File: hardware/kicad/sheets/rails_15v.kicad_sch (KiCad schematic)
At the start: 31 parts, among them U10 ADP7182AUJZ, U8 ADP5071AREZ, U9 ADP7142AUJZ

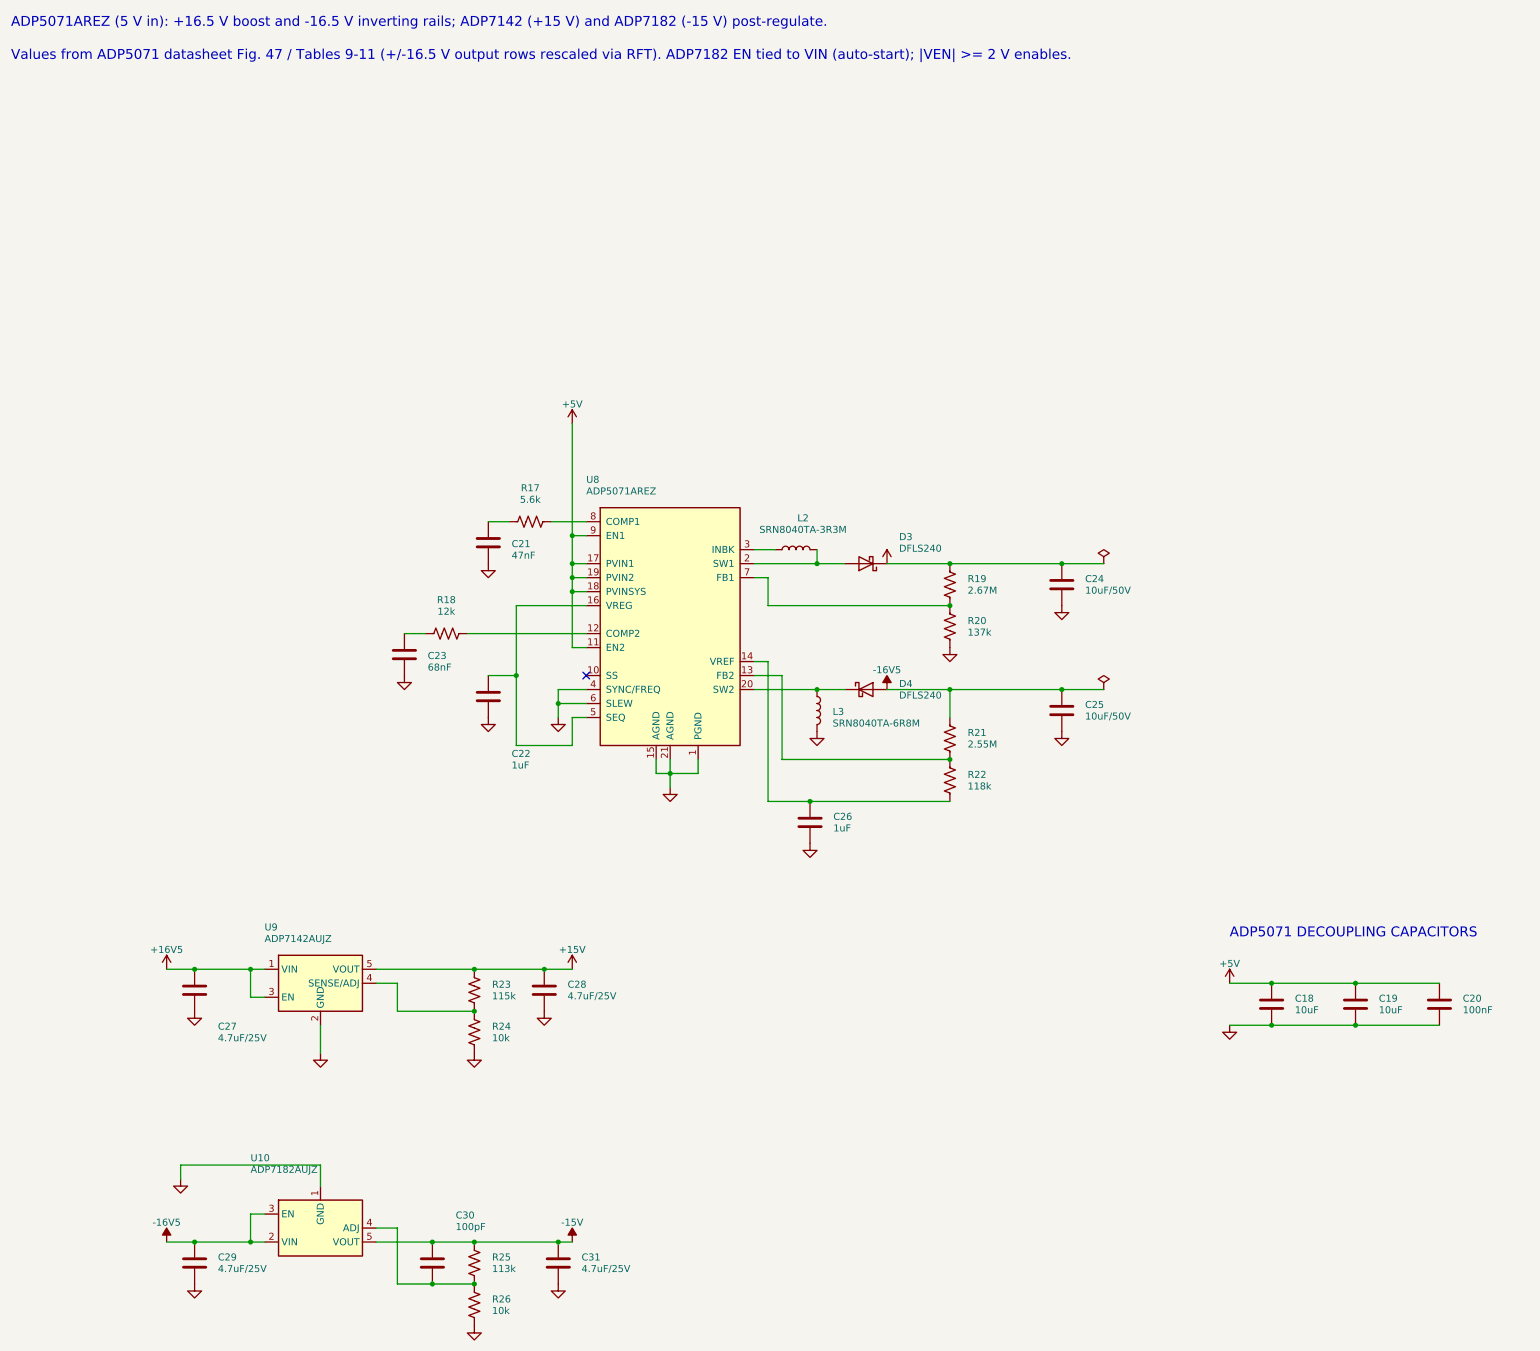
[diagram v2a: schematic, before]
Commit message: Fixing the UUID issues
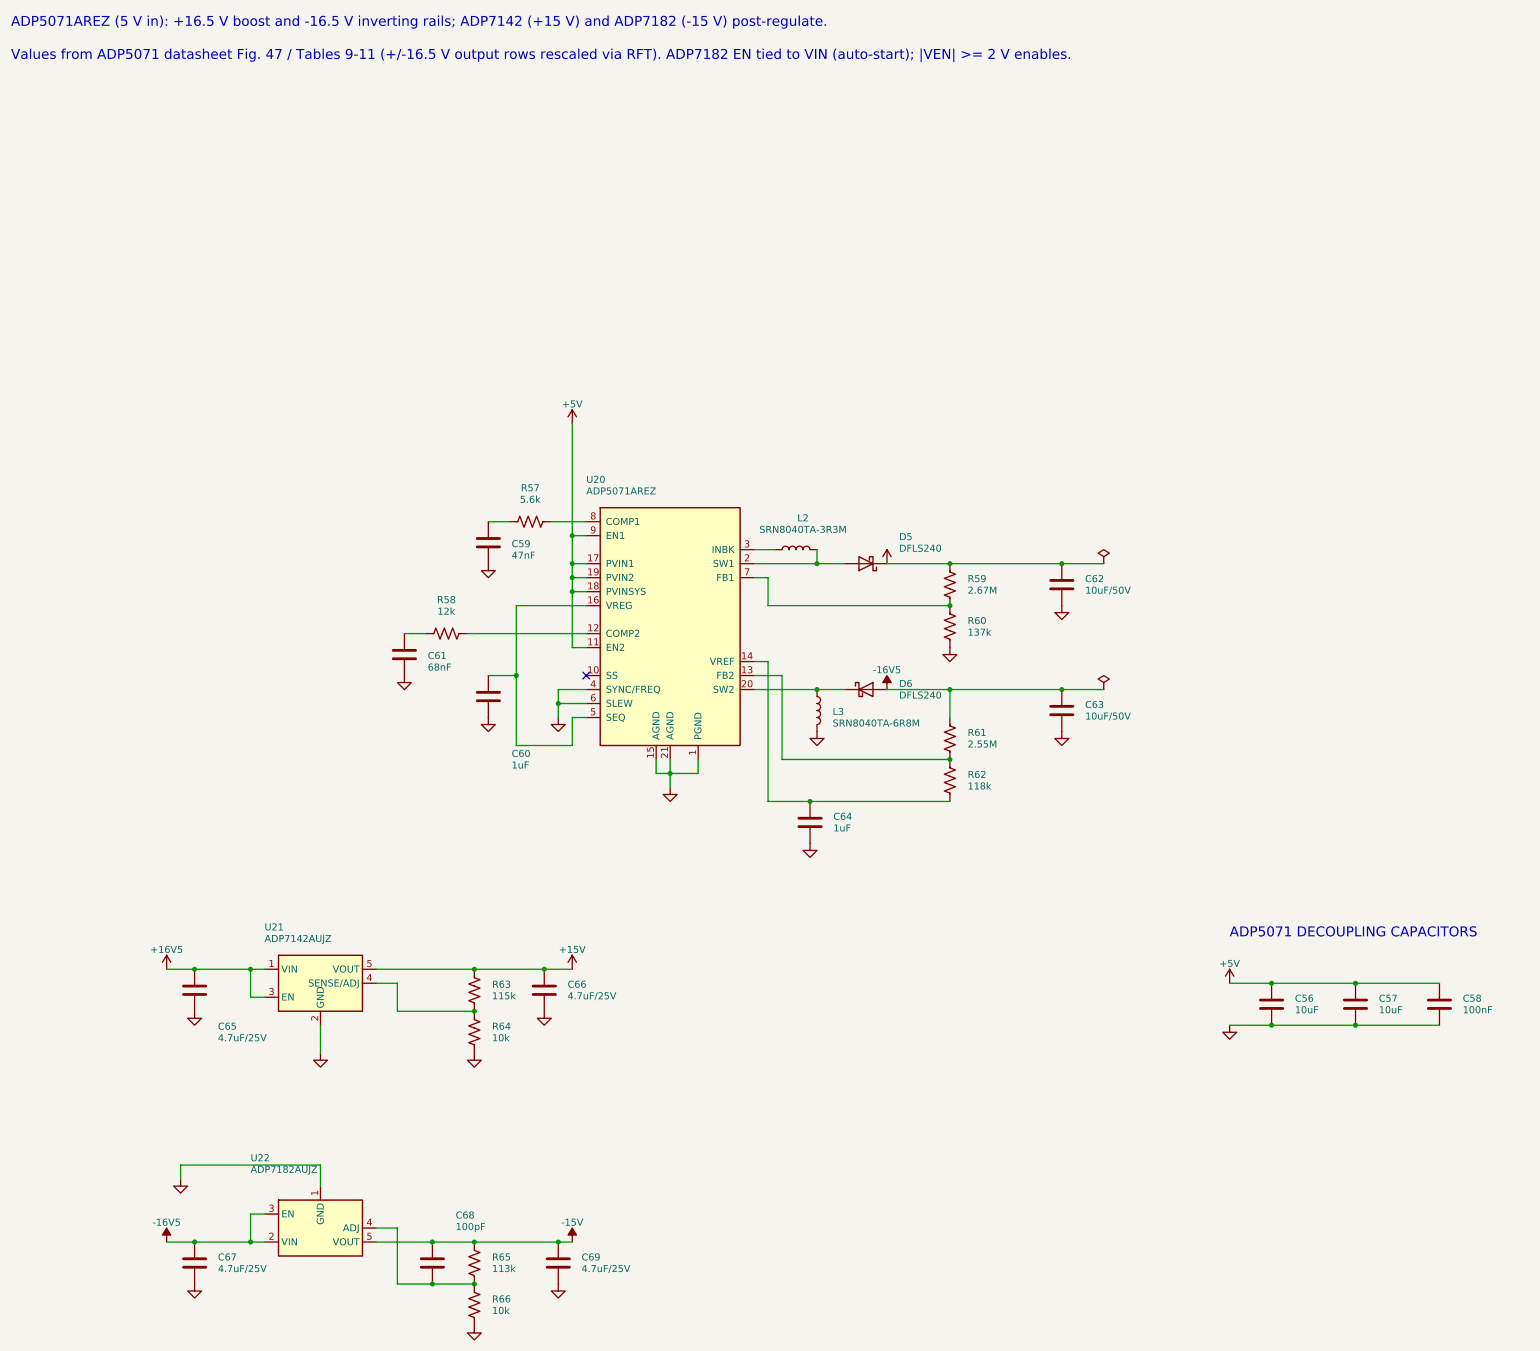
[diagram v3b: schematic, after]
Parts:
- removed C18, C19: 10uF, Capacitor_SMD:C_0805_2012Metric, symbol Device:C
- removed C20: 100nF, Capacitor_SMD:C_0603_1608Metric, symbol Device:C
- removed C21: 47nF, Capacitor_SMD:C_1206_3216Metric, symbol Device:C
- removed C22, C26: 1uF, Capacitor_SMD:C_0805_2012Metric, symbol Device:C
- removed C23: 68nF, Capacitor_SMD:C_1206_3216Metric, symbol Device:C
- removed C24, C25: 10uF/50V, Capacitor_SMD:C_1210_3225Metric, symbol Device:C
- removed C27, C28, C29, C31: 4.7uF/25V, Capacitor_SMD:C_1206_3216Metric, symbol Device:C
- removed C30: 100pF, Capacitor_SMD:C_1206_3216Metric, symbol Device:C
- removed D3, D4: DFLS240, Diode_SMD:D_PowerDI-123, symbol Device:D_Schottky
- removed R17: 5.6k, Resistor_SMD:R_0603_1608Metric, symbol Device:R_US
- removed R18: 12k, Resistor_SMD:R_0603_1608Metric, symbol Device:R_US
- removed R19: 2.67M, Resistor_SMD:R_0603_1608Metric, symbol Device:R_US
- removed R20: 137k, Resistor_SMD:R_0603_1608Metric, symbol Device:R_US
- removed R21: 2.55M, Resistor_SMD:R_0603_1608Metric, symbol Device:R_US
- removed R22: 118k, Resistor_SMD:R_0603_1608Metric, symbol Device:R_US
- removed R23: 115k, Resistor_SMD:R_0603_1608Metric, symbol Device:R_US
- removed R24, R26: 10k, Resistor_SMD:R_0603_1608Metric, symbol Device:R_US
- removed R25: 113k, Resistor_SMD:R_0603_1608Metric, symbol Device:R_US
- removed U10: ADP7182AUJZ, Package_TO_SOT_SMD:TSOT-23-5, symbol Regulator_Linear:ADP7182AUJZ
- removed U8: ADP5071AREZ, Package_SO:ETSSOP-20-1EP_4.4x6.5mm_P0.65mm_EP3x4.2mm, symbol Regulator_Switching:ADP5071AREZ
- removed U9: ADP7142AUJZ, Package_TO_SOT_SMD:TSOT-23-5, symbol Regulator_Linear:ADP7142AUJZ
- added C56, C57: 10uF, Capacitor_SMD:C_0805_2012Metric, symbol Device:C
- added C58: 100nF, Capacitor_SMD:C_0603_1608Metric, symbol Device:C
- added C59: 47nF, Capacitor_SMD:C_1206_3216Metric, symbol Device:C
- added C60, C64: 1uF, Capacitor_SMD:C_0805_2012Metric, symbol Device:C
- added C61: 68nF, Capacitor_SMD:C_1206_3216Metric, symbol Device:C
- added C62, C63: 10uF/50V, Capacitor_SMD:C_1210_3225Metric, symbol Device:C
- added C65, C66, C67, C69: 4.7uF/25V, Capacitor_SMD:C_1206_3216Metric, symbol Device:C
- added C68: 100pF, Capacitor_SMD:C_1206_3216Metric, symbol Device:C
- added D5, D6: DFLS240, Diode_SMD:D_PowerDI-123, symbol Device:D_Schottky
- added R57: 5.6k, Resistor_SMD:R_0603_1608Metric, symbol Device:R_US
- added R58: 12k, Resistor_SMD:R_0603_1608Metric, symbol Device:R_US
- added R59: 2.67M, Resistor_SMD:R_0603_1608Metric, symbol Device:R_US
- added R60: 137k, Resistor_SMD:R_0603_1608Metric, symbol Device:R_US
- added R61: 2.55M, Resistor_SMD:R_0603_1608Metric, symbol Device:R_US
- added R62: 118k, Resistor_SMD:R_0603_1608Metric, symbol Device:R_US
- added R63: 115k, Resistor_SMD:R_0603_1608Metric, symbol Device:R_US
- added R64, R66: 10k, Resistor_SMD:R_0603_1608Metric, symbol Device:R_US
- added R65: 113k, Resistor_SMD:R_0603_1608Metric, symbol Device:R_US
- added U20: ADP5071AREZ, Package_SO:ETSSOP-20-1EP_4.4x6.5mm_P0.65mm_EP3x4.2mm, symbol Regulator_Switching:ADP5071AREZ
- added U21: ADP7142AUJZ, Package_TO_SOT_SMD:TSOT-23-5, symbol Regulator_Linear:ADP7142AUJZ
- added U22: ADP7182AUJZ, Package_TO_SOT_SMD:TSOT-23-5, symbol Regulator_Linear:ADP7182AUJZ
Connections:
- net +15V: now also C66.1, R63.1, U21.5 (VOUT)
- net +16V5: now also C62.1, C65.1, D5.1 (K), R59.1, U21.1 (VIN), U21.3 (EN)
- net +5V: now also C56.1, C57.1, C58.1, U20.11 (EN2), U20.17 (PVIN1), U20.18 (PVINSYS), U20.19 (PVIN2), U20.9 (EN1)
- net -15V: now also C68.1, C69.1, R65.1, U22.5 (VOUT)
- net -16V5: now also C63.1, C67.1, D6.2 (A), R61.1, U22.2 (VIN), U22.3 (EN)
- net GND: now also C56.2, C57.2, C58.2, C59.2, C60.2, C61.2, C62.2, C63.2, C64.2, C65.2, C66.2, C67.2, C69.2, R60.2, R64.2, R66.2, U20.1 (PGND), U20.15 (AGND), U20.21 (AGND), U20.4 (SYNC/FREQ), U20.6 (SLEW), U21.2 (GND), U22.1 (GND)
- net at L3.1: now also D6.1 (K), U20.20 (SW2)
- net at L2.2: now also D5.2 (A), U20.2 (SW1)
- net at L2.1: now also U20.3 (INBK)
- new net: C61.1, R58.1
- new net: R58.2, U20.12 (COMP2)
- new net: R63.2, R64.1, U21.4 (SENSE/ADJ)
- new net: C68.2, R65.2, R66.1, U22.4 (ADJ)
- new net: C59.1, R57.1
- new net: R57.2, U20.8 (COMP1)
- new net: C60.1, U20.16 (VREG), U20.5 (SEQ)
- new net: C64.1, R62.2, U20.14 (VREF)
- new net: R59.2, R60.1, U20.7 (FB1)
- new net: R61.2, R62.1, U20.13 (FB2)
